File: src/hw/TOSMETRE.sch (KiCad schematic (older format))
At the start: 54 parts, among them J1 Alim, J2 Conn_Coaxial, J3 Conn_01x08_Male, J5 Conn_Coaxial, U1 18F1320, U2 L7805, U3 LT1818, U4 AD5175, U5 LTC2305, U6 LT1818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

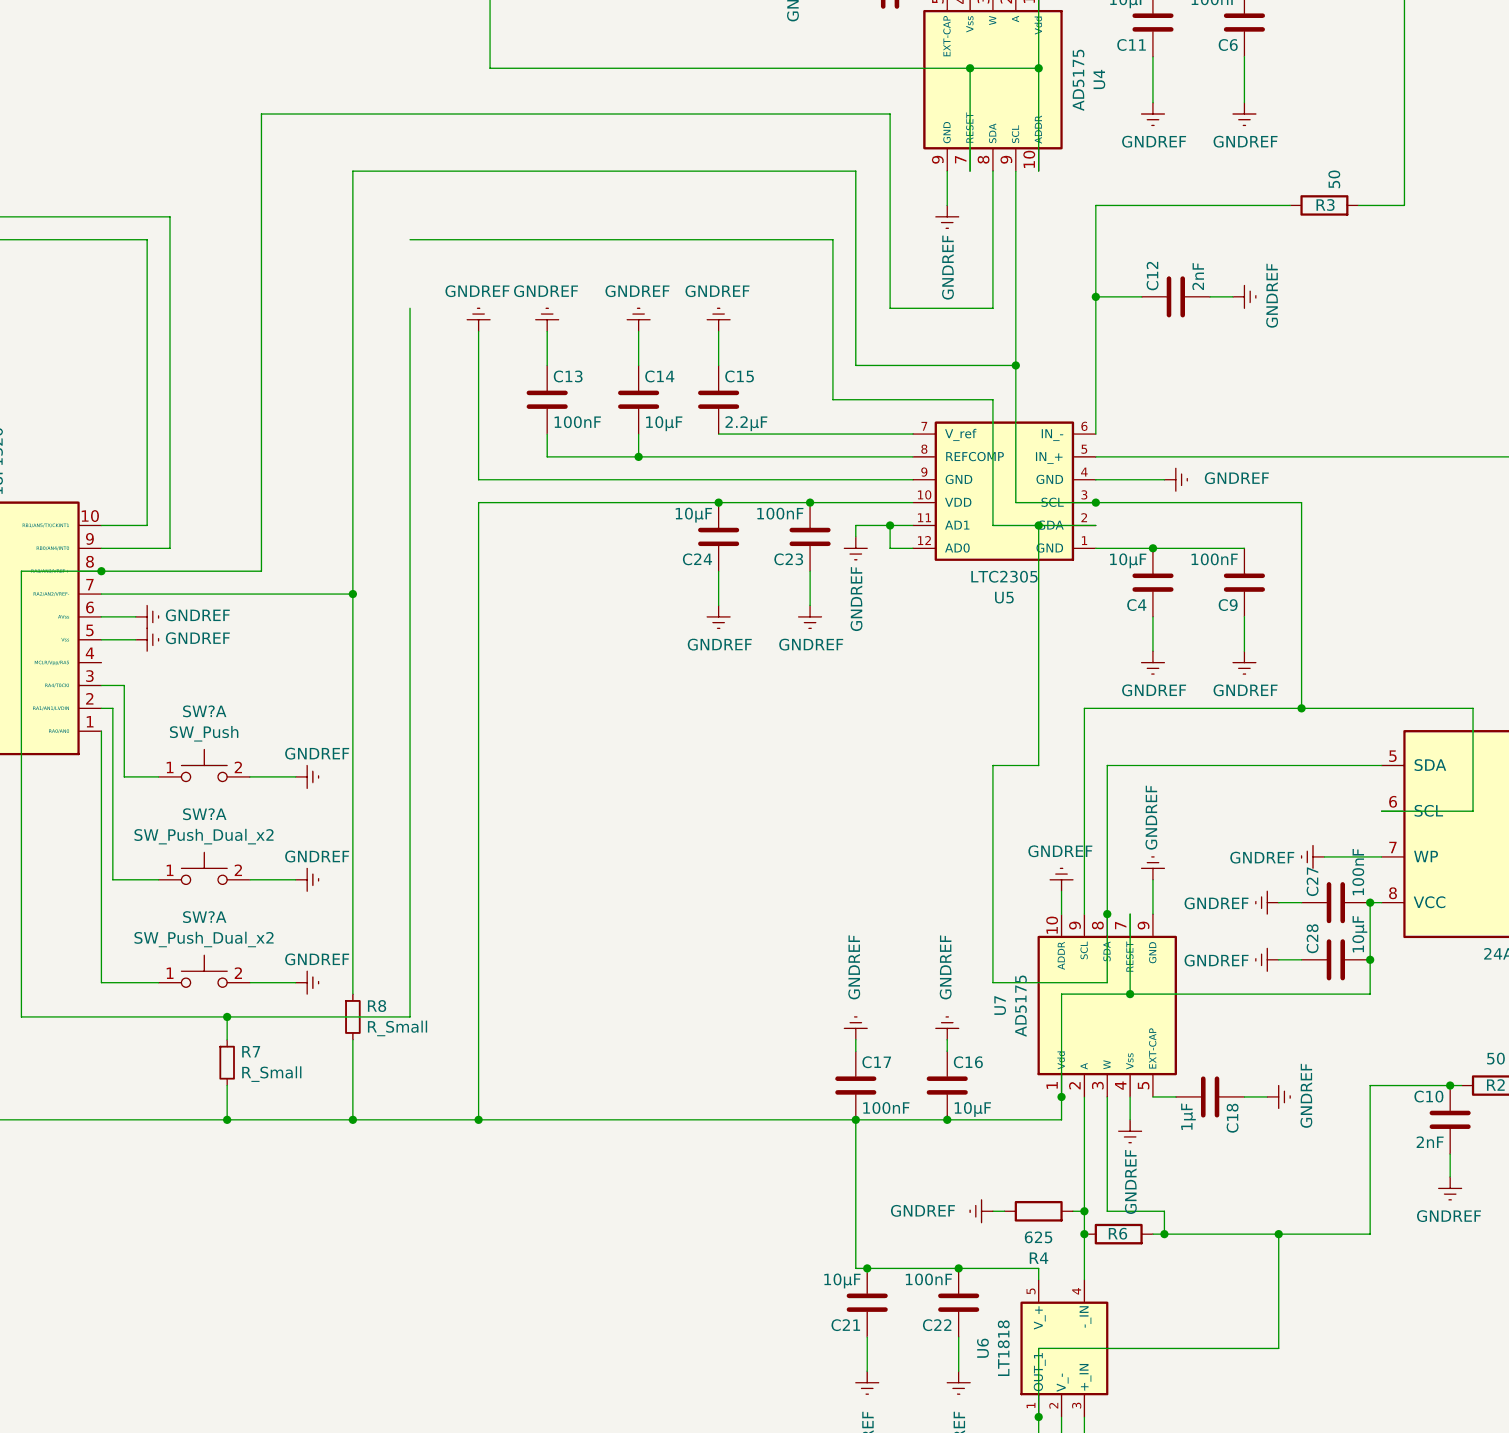
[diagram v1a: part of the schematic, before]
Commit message: #307
Mise a jour des empreintes pour le schema
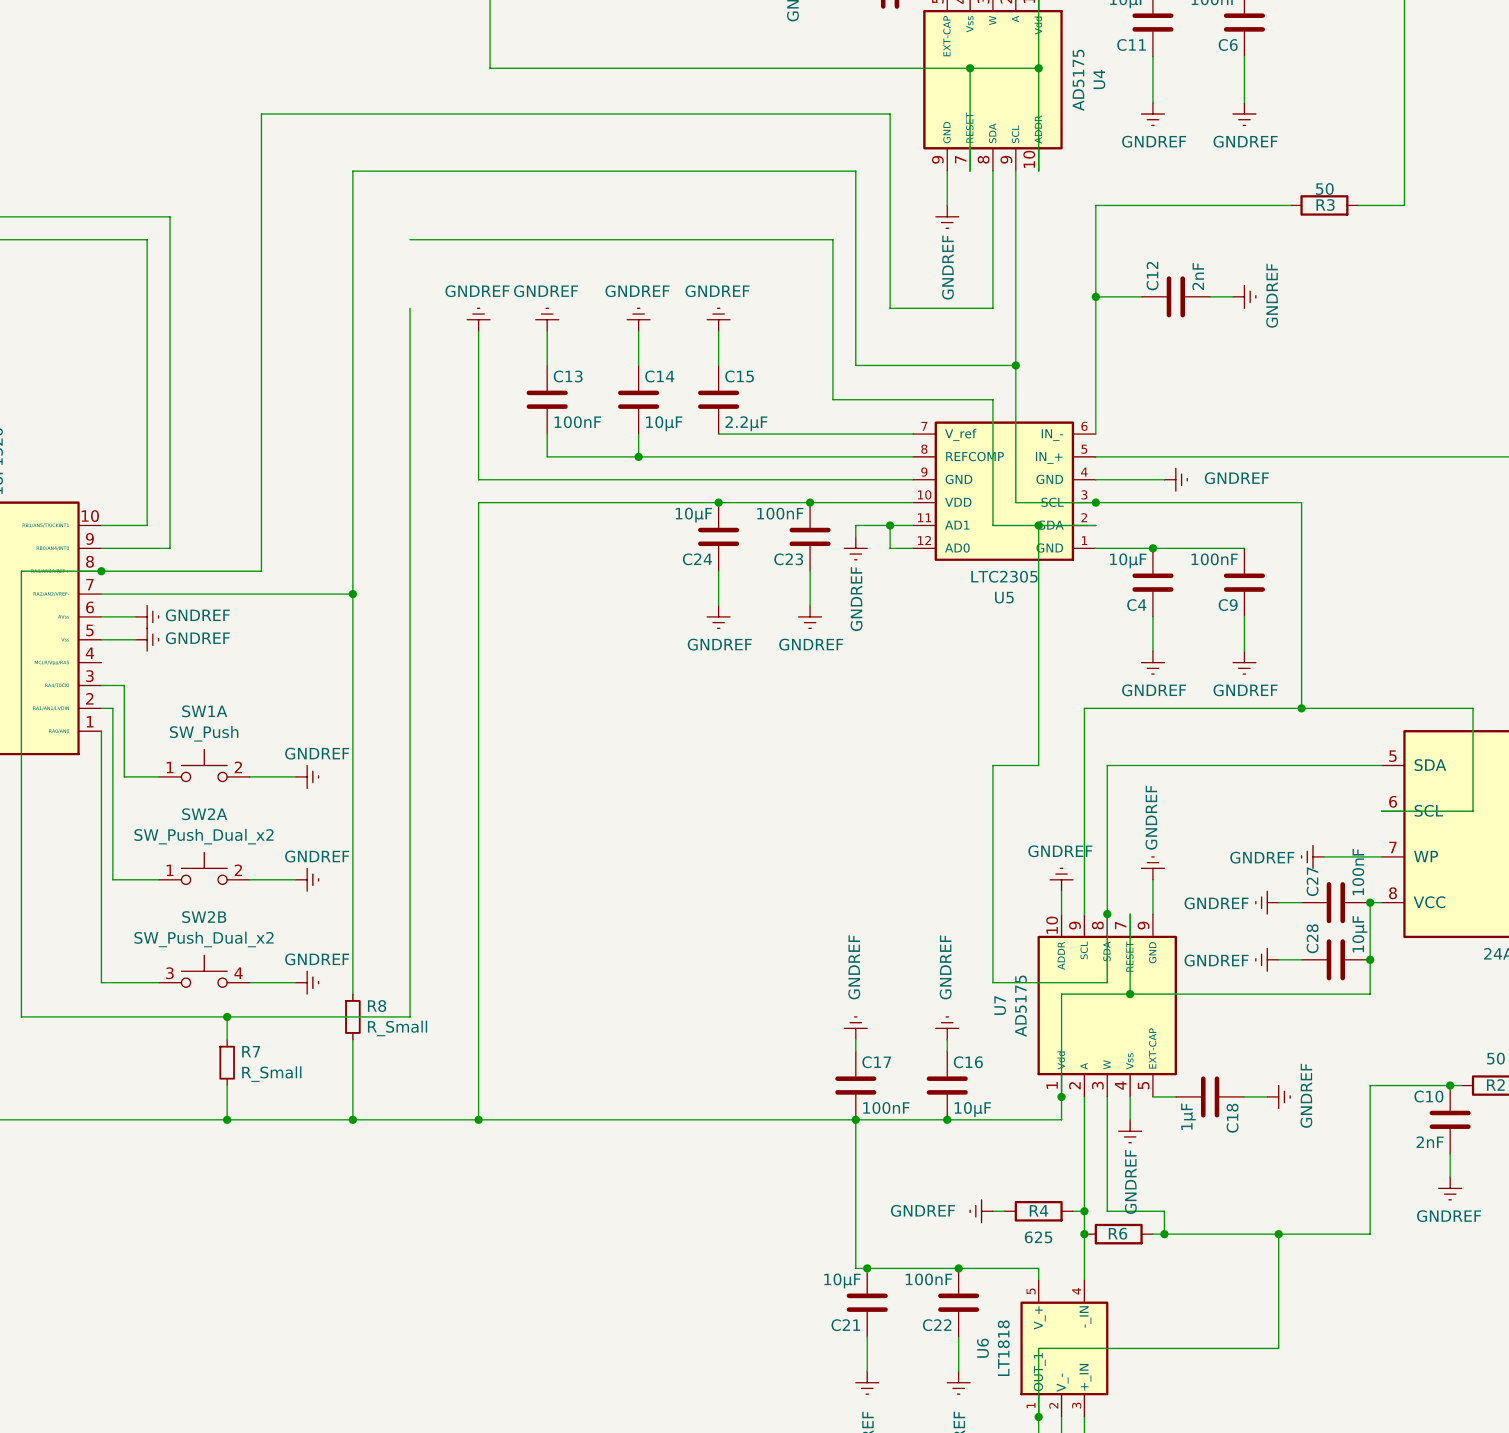
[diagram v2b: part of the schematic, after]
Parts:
- J3: footprint (none) -> Connector_PinHeader_2.00mm:PinHeader_1x08_P2.00mm_Vertical
- R1, R2, R3, R4, R5, R6, R7, R8: footprint (none) -> Resistor_SMD:R_1206_3216Metric
- SW1, SW2: renamed from SW?; footprint (none) -> Button_Switch_SMD:SW_Push_1P1T-SH_NO_CK_KMR2xxG
- U8: footprint (none) -> Package_SO:TSSOP-8_3x3mm_P0.65mm
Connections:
- net GNDREF: now also SW2.4 (D); no longer SW2.2 (D)
- net at U1.1 (RA0/AN0): now also SW2.3 (C); no longer SW2.1 (C)
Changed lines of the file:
@@
 P 10750 4500
 F 0 "R3" V 10750 4450 50  0000 L CNN
-F 1 "50" H 10820 4455 50  0000 L CNN
-F 2 "" V 10680 4500 50  0001 C CNN
+F 1 "50" V 10820 4455 50  0000 L CNN
+F 2 "Resistor_SMD:R_1206_3216Metric" V 10680 4500 50  0001 C CNN
 F 3 "~" H 10750 4500 50  0001 C CNN
 	1    10750 4500
@@
 F 0 "R1" V 9600 3150 50  0000 L CNN
 F 1 "625" H 9670 3155 50  0000 L CNN
-F 2 "" V 9530 3200 50  0001 C CNN
+F 2 "Resistor_SMD:R_1206_3216Metric" V 9530 3200 50  0001 C CNN
 F 3 "~" H 9600 3200 50  0001 C CNN
 	1    9600 3200
@@
 F 0 "R5" V 9200 3000 50  0000 L CNN
 F 1 " " H 9270 3005 50  0000 L CNN
-F 2 "" V 9130 3050 50  0001 C CNN
+F 2 "Resistor_SMD:R_1206_3216Metric" V 9130 3050 50  0001 C CNN
 F 3 "~" H 9200 3050 50  0001 C CNN
 	1    9200 3050
@@
 F 0 "J3" H 3172 4632 50  0000 R CNN
 F 1 "Conn_01x08_Male" H 3172 4723 50  0000 R CNN
-F 2 "" H 3200 4750 50  0001 C CNN
+F 2 "Connector_PinHeader_2.00mm:PinHeader_1x08_P2.00mm_Vertical" H 3200 4750 50  0001 C CNN
 F 3 "~" H 3200 4750 50  0001 C CNN
 	1    3200 4750
@@
 F 0 "R6" V 9850 9050 50  0000 R CNN
 F 1 " " V 9734 9000 50  0000 C CNN
-F 2 "" V 9780 9000 50  0001 C CNN
+F 2 "Resistor_SMD:R_1206_3216Metric" V 9780 9000 50  0001 C CNN
 F 3 "~" H 9850 9000 50  0001 C CNN
 	1    9850 9000
@@
 F 0 "R2" V 11500 8350 50  0000 C CNN
 F 1 "50" V 11384 8350 50  0000 C CNN
-F 2 "" V 11430 8350 50  0001 C CNN
+F 2 "Resistor_SMD:R_1206_3216Metric" V 11430 8350 50  0001 C CNN
 F 3 "~" H 11500 8350 50  0001 C CNN
 	1    11500 8350
@@
 F 0 "R8" H 6559 8096 50  0000 L CNN
 F 1 "R_Small" H 6559 8005 50  0000 L CNN
-F 2 "" H 6500 8050 50  0001 C CNN
+F 2 "Resistor_SMD:R_1206_3216Metric" H 6500 8050 50  0001 C CNN
 F 3 "~" H 6500 8050 50  0001 C CNN
 	1    6500 8050
@@
 F 0 "R7" H 6009 8296 50  0000 L CNN
 F 1 "R_Small" H 6009 8205 50  0000 L CNN
-F 2 "" H 5950 8250 50  0001 C CNN
+F 2 "Resistor_SMD:R_1206_3216Metric" H 5950 8250 50  0001 C CNN
 F 3 "~" H 5950 8250 50  0001 C CNN
 	1    5950 8250
@@
 	9300 5900 9500 5900
 Connection ~ 9500 5900
-$Comp
-L librairie_projet:24AA256 U8
-U 1 1 5ED2FD7E
-P 11600 7250
-F 0 "U8" H 11600 7867 50  0000 C CNN
-F 1 "24AA256" H 11600 7776 50  0000 C CNN
-F 2 "" H 11600 7250 50  0001 C CNN
-F 3 "http://www.nxp.com/documents/data_sheet/P82B96.pdf" H 11600 7250 50  0001 C CNN
-	1    11600 7250
-	-1   0    0    1
-$EndComp
 Connection ~ 9800 7600
 Wire Wire Line
@@
 U 1 1 5EC4DB73
 P 9500 8900
-F 0 "R4" V 9293 8900 50  0000 C CNN
+F 0 "R4" V 9500 8900 50  0000 C CNN
 F 1 "625" V 9384 8900 50  0000 C CNN
-F 2 "" V 9430 8900 50  0001 C CNN
+F 2 "Resistor_SMD:R_1206_3216Metric" V 9430 8900 50  0001 C CNN
 F 3 "~" H 9500 8900 50  0001 C CNN
 	1    9500 8900
@@
 	5500 6600 5500 7000
 $Comp
-L power:GNDREF #PWR?
+L power:GNDREF #PWR0149
 U 1 1 5F2AF3C5
 P 6250 7000
-F 0 "#PWR?" H 6250 6750 50  0001 C CNN
+F 0 "#PWR0149" H 6250 6750 50  0001 C CNN
 F 1 "GNDREF" V 6350 7050 50  0000 R CNN
 F 2 "" H 6250 7000 50  0001 C CNN
@@
 $EndComp
 $Comp
-L power:GNDREF #PWR?
+L power:GNDREF #PWR0150
 U 1 1 5F2B062F
 P 6250 7450
-F 0 "#PWR?" H 6250 7200 50  0001 C CNN
+F 0 "#PWR0150" H 6250 7200 50  0001 C CNN
 F 1 "GNDREF" V 6350 7500 50  0000 R CNN
 F 2 "" H 6250 7450 50  0001 C CNN
@@
 $EndComp
 $Comp
-L power:GNDREF #PWR?
+L power:GNDREF #PWR0151
 U 1 1 5F2B0FD4
 P 6250 7900
-F 0 "#PWR?" H 6250 7650 50  0001 C CNN
+F 0 "#PWR0151" H 6250 7650 50  0001 C CNN
 F 1 "GNDREF" V 6350 7950 50  0000 R CNN
 F 2 "" H 6250 7900 50  0001 C CNN
@@
 FWD\n
 $Comp
-L Switch:SW_Push_Dual_x2 SW?
+L Switch:SW_Push_Dual_x2 SW1
 U 1 1 602CE788
 P 5850 7000
-F 0 "SW?" H 5850 7285 50  0000 C CNN
+F 0 "SW1" H 5850 7285 50  0000 C CNN
 F 1 "SW_Push" H 5850 7194 50  0000 C CNN
-F 2 "" H 5850 7200 50  0001 C CNN
+F 2 "Button_Switch_SMD:SW_Push_1P1T-SH_NO_CK_KMR2xxG" H 5850 7200 50  0001 C CNN
 F 3 "~" H 5850 7200 50  0001 C CNN
 	1    5850 7000
@@
 $EndComp
 $Comp
-L Switch:SW_Push_Dual_x2 SW?
+L Switch:SW_Push_Dual_x2 SW2
 U 1 1 602F02F4
 P 5850 7450
-F 0 "SW?" H 5850 7735 50  0000 C CNN
+F 0 "SW2" H 5850 7735 50  0000 C CNN
 F 1 "SW_Push_Dual_x2" H 5850 7644 50  0000 C CNN
-F 2 "" H 5850 7650 50  0001 C CNN
+F 2 "Button_Switch_SMD:SW_Push_1P1T-SH_NO_CK_KMR2xxG" H 5850 7650 50  0001 C CNN
 F 3 "~" H 5850 7650 50  0001 C CNN
 	1    5850 7450
@@
 $EndComp
 $Comp
-L Switch:SW_Push_Dual_x2 SW?
-U 1 1 602F1015
+L Switch:SW_Push_Dual_x2 SW2
+U 2 1 602F1015
 P 5850 7900
-F 0 "SW?" H 5850 8185 50  0000 C CNN
+F 0 "SW2" H 5850 8185 50  0000 C CNN
 F 1 "SW_Push_Dual_x2" H 5850 8094 50  0000 C CNN
-F 2 "" H 5850 8100 50  0001 C CNN
+F 2 "Button_Switch_SMD:SW_Push_1P1T-SH_NO_CK_KMR2xxG" H 5850 8100 50  0001 C CNN
 F 3 "~" H 5850 8100 50  0001 C CNN
-	1    5850 7900
+	2    5850 7900
 	1    0    0    -1
 $EndComp
@@
 Wire Wire Line
 	5450 6700 5450 7450
+$Comp
+L librairie_projet:24AA256 U8
+U 1 1 5ED2FD7E
+P 11600 7250
+F 0 "U8" H 11600 7867 50  0000 C CNN
+F 1 "24AA256" H 11600 7776 50  0000 C CNN
+F 2 "Package_SO:TSSOP-8_3x3mm_P0.65mm" H 11600 7250 50  0001 C CNN
+F 3 "http://www.nxp.com/documents/data_sheet/P82B96.pdf" H 11600 7250 50  0001 C CNN
+	1    11600 7250
+	-1   0    0    1
+$EndComp
 $EndSCHEMATC

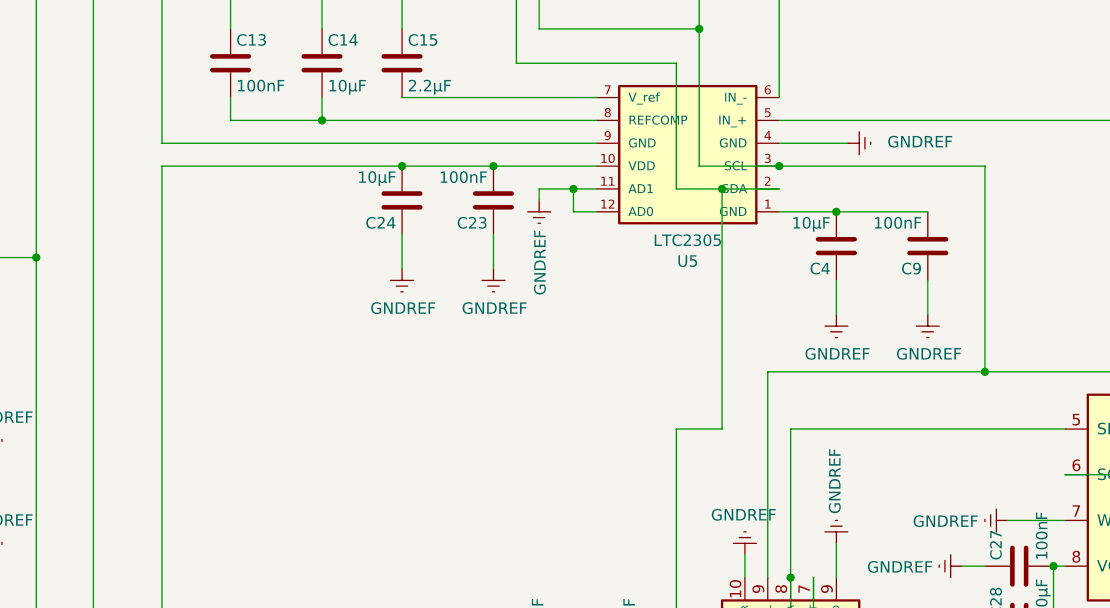
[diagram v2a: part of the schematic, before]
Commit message: #299
#299 deplacement capa de decouplage
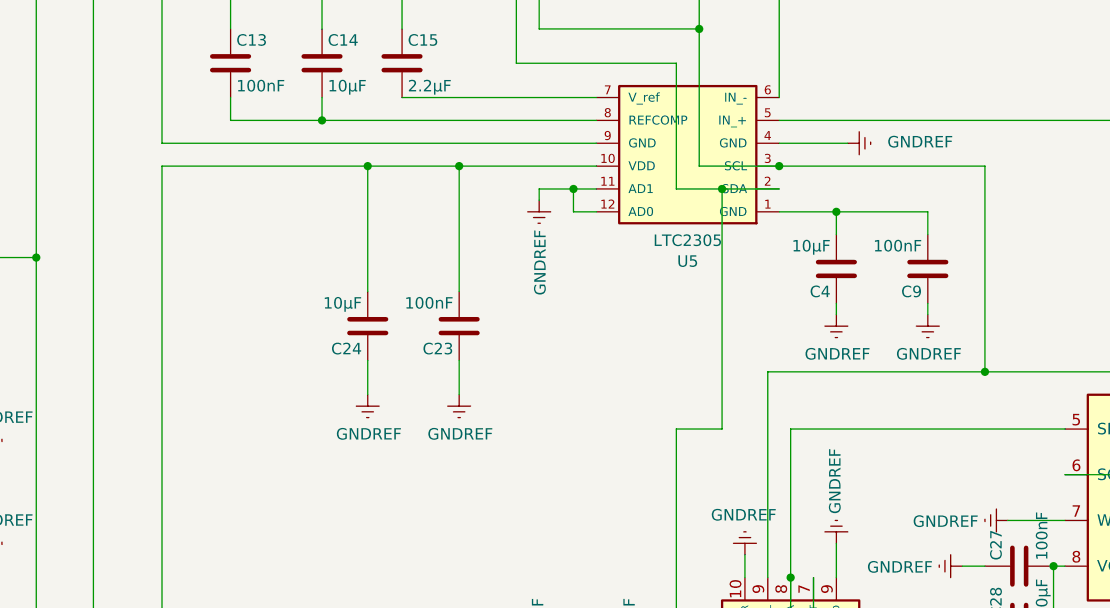
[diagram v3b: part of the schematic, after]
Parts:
- U8: footprint Package_SO:TSSOP-8_3x3mm_P0.65mm -> Package_SO:TSSOP-8_4.4x3mm_P0.65mm
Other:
- moved on the sheet: C23, C24, C4, C9
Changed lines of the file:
@@
 	-1   0    0    1
 $EndComp
-Connection ~ 10000 6000
-Wire Wire Line
-	9750 6000 10000 6000
 $Comp
 L Device:C C9
 U 1 1 5ED2AB54
-P 10400 6150
-F 0 "C9" H 10425 6250 50  0000 L CNN
-F 1 "100nF" H 10425 6050 50  0000 L CNN
-F 2 "Capacitor_SMD:C_1206_3216Metric" H 10438 6000 50  0001 C CNN
-F 3 "" H 10400 6150 50  0001 C CNN
-	1    10400 6150
+P 10400 6250
+F 0 "C9" H 10425 6350 50  0000 L CNN
+F 1 "100nF" H 10425 6150 50  0000 L CNN
+F 2 "Capacitor_SMD:C_1206_3216Metric" H 10438 6100 50  0001 C CNN
+F 3 "" H 10400 6250 50  0001 C CNN
+	1    10400 6250
 	-1   0    0    1
 $EndComp
@@
 	1    0    0    -1
 $EndComp
-Wire Wire Line
-	10400 6300 10400 6450
-Wire Wire Line
-	10000 6000 10400 6000
-Wire Wire Line
-	10000 6450 10000 6300
 $Comp
 L Device:C C4
 U 1 1 5ED2AB6B
-P 10000 6150
-F 0 "C4" H 10025 6250 50  0000 L CNN
-F 1 "10µF" H 10025 6050 50  0000 L CNN
-F 2 "Capacitor_SMD:C_1206_3216Metric" H 10038 6000 50  0001 C CNN
-F 3 "" H 10000 6150 50  0001 C CNN
-	1    10000 6150
-	-1   0    0    1
-$EndComp
-Connection ~ 8500 5800
-Wire Wire Line
-	8950 5800 8500 5800
+P 10000 6250
+F 0 "C4" H 10025 6350 50  0000 L CNN
+F 1 "10µF" H 10025 6150 50  0000 L CNN
+F 2 "Capacitor_SMD:C_1206_3216Metric" H 10038 6100 50  0001 C CNN
+F 3 "" H 10000 6250 50  0001 C CNN
+	1    10000 6250
+	-1   0    0    1
+$EndComp
 $Comp
 L Device:C C24
 U 1 1 5ED64B7D
-P 8100 5950
-F 0 "C24" H 8125 6050 50  0000 L CNN
-F 1 "10µF" H 8125 5850 50  0000 L CNN
-F 2 "Capacitor_SMD:C_1206_3216Metric" H 8138 5800 50  0001 C CNN
-F 3 "" H 8100 5950 50  0001 C CNN
-	1    8100 5950
-	-1   0    0    1
-$EndComp
-Wire Wire Line
-	8100 6250 8100 6100
-Wire Wire Line
-	8100 5800 8500 5800
-Wire Wire Line
-	8500 6100 8500 6250
+P 7950 6500
+F 0 "C24" H 7975 6600 50  0000 L CNN
+F 1 "10µF" H 7975 6400 50  0000 L CNN
+F 2 "Capacitor_SMD:C_1206_3216Metric" H 7988 6350 50  0001 C CNN
+F 3 "" H 7950 6500 50  0001 C CNN
+	1    7950 6500
+	-1   0    0    1
+$EndComp
+Wire Wire Line
+	7950 6800 7950 6650
+Wire Wire Line
+	8350 6650 8350 6800
 $Comp
 L power:GNDREF #PWR0134
 U 1 1 5ED64B72
-P 8100 6250
-F 0 "#PWR0134" H 8100 6000 50  0001 C CNN
-F 1 "GNDREF" H 8105 6077 50  0000 C CNN
-F 2 "" H 8100 6250 50  0001 C CNN
-F 3 "" H 8100 6250 50  0001 C CNN
-	1    8100 6250
+P 7950 6800
+F 0 "#PWR0134" H 7950 6550 50  0001 C CNN
+F 1 "GNDREF" H 7955 6627 50  0000 C CNN
+F 2 "" H 7950 6800 50  0001 C CNN
+F 3 "" H 7950 6800 50  0001 C CNN
+	1    7950 6800
 	1    0    0    -1
 $EndComp
@@
 L power:GNDREF #PWR0133
 U 1 1 5ED64B6C
-P 8500 6250
-F 0 "#PWR0133" H 8500 6000 50  0001 C CNN
-F 1 "GNDREF" H 8505 6077 50  0000 C CNN
-F 2 "" H 8500 6250 50  0001 C CNN
-F 3 "" H 8500 6250 50  0001 C CNN
-	1    8500 6250
+P 8350 6800
+F 0 "#PWR0133" H 8350 6550 50  0001 C CNN
+F 1 "GNDREF" H 8355 6627 50  0000 C CNN
+F 2 "" H 8350 6800 50  0001 C CNN
+F 3 "" H 8350 6800 50  0001 C CNN
+	1    8350 6800
 	1    0    0    -1
 $EndComp
@@
 L Device:C C23
 U 1 1 5ED64B66
-P 8500 5950
-F 0 "C23" H 8525 6050 50  0000 L CNN
-F 1 "100nF" H 8525 5850 50  0000 L CNN
-F 2 "Capacitor_SMD:C_1206_3216Metric" H 8538 5800 50  0001 C CNN
-F 3 "" H 8500 5950 50  0001 C CNN
-	1    8500 5950
+P 8350 6500
+F 0 "C23" H 8375 6600 50  0000 L CNN
+F 1 "100nF" H 8375 6400 50  0000 L CNN
+F 2 "Capacitor_SMD:C_1206_3216Metric" H 8388 6350 50  0001 C CNN
+F 3 "" H 8350 6500 50  0001 C CNN
+	1    8350 6500
 	-1   0    0    1
 $EndComp
@@
 Wire Wire Line
 	9400 5800 9750 5800
-Connection ~ 8100 5800
 Wire Wire Line
 	6100 4100 6100 6100
@@
 Wire Wire Line
 	6100 4100 8850 4100
-Wire Wire Line
-	7050 5800 8100 5800
 Wire Wire Line
 	6500 6200 6500 4350
@@
 F 0 "U8" H 11600 7867 50  0000 C CNN
 F 1 "24AA256" H 11600 7776 50  0000 C CNN
-F 2 "Package_SO:TSSOP-8_3x3mm_P0.65mm" H 11600 7250 50  0001 C CNN
+F 2 "Package_SO:TSSOP-8_4.4x3mm_P0.65mm" H 11600 7250 50  0001 C CNN
 F 3 "http://www.nxp.com/documents/data_sheet/P82B96.pdf" H 11600 7250 50  0001 C CNN
 	1    11600 7250
 	-1   0    0    1
 $EndComp
+Wire Wire Line
+	7050 5800 7950 5800
+Wire Wire Line
+	7950 6350 7950 5800
+Connection ~ 7950 5800
+Wire Wire Line
+	7950 5800 8350 5800
+Wire Wire Line
+	8350 6350 8350 5800
+Connection ~ 8350 5800
+Wire Wire Line
+	8350 5800 8950 5800
+Wire Wire Line
+	10400 6400 10400 6450
+Wire Wire Line
+	9750 6000 10000 6000
+Wire Wire Line
+	10000 6450 10000 6400
+Wire Wire Line
+	10000 6100 10000 6000
+Connection ~ 10000 6000
+Wire Wire Line
+	10000 6000 10400 6000
+Wire Wire Line
+	10400 6000 10400 6100
 $EndSCHEMATC
